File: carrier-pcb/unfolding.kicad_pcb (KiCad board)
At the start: 2 copper layers, 66 parts, among them J1 USB_C_Receptacle_USB2.0, J2 Conn_01x04_Female, J3 CONN_1-338068-8_TYC, U1 TCA9548APWR, U10 DRV2605LDGS, U11 DRV2605LDGS, U12 BMX160, U2 TCA9548APWR, U3 DRV2605LDGS, U4 DRV2605LDGS, U5 DRV2605LDGS, U6 DRV2605LDGS, U7 DRV2605LDGS, U8 DRV2605LDGS, U9 DRV2605LDGS

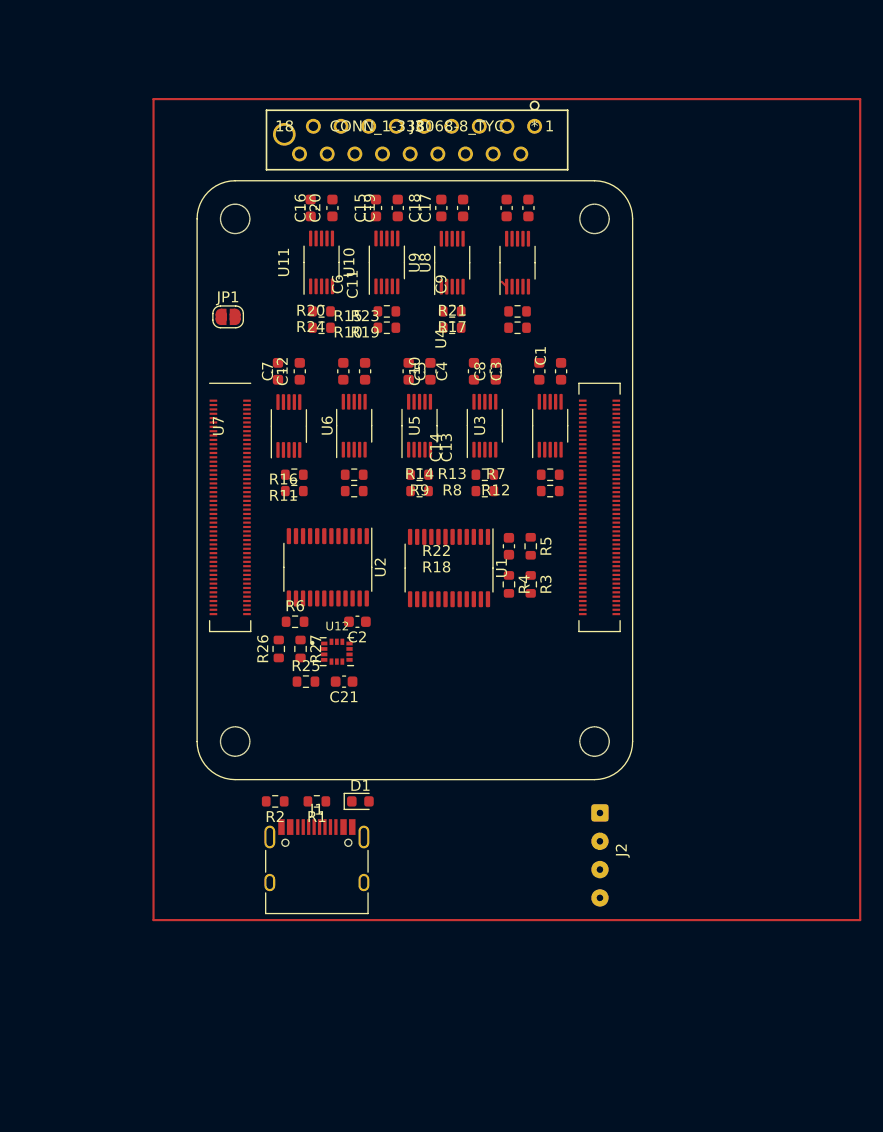
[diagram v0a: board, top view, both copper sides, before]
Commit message: removed more backups and renamed files. USE MORE BRANCHES, DONT RENAME
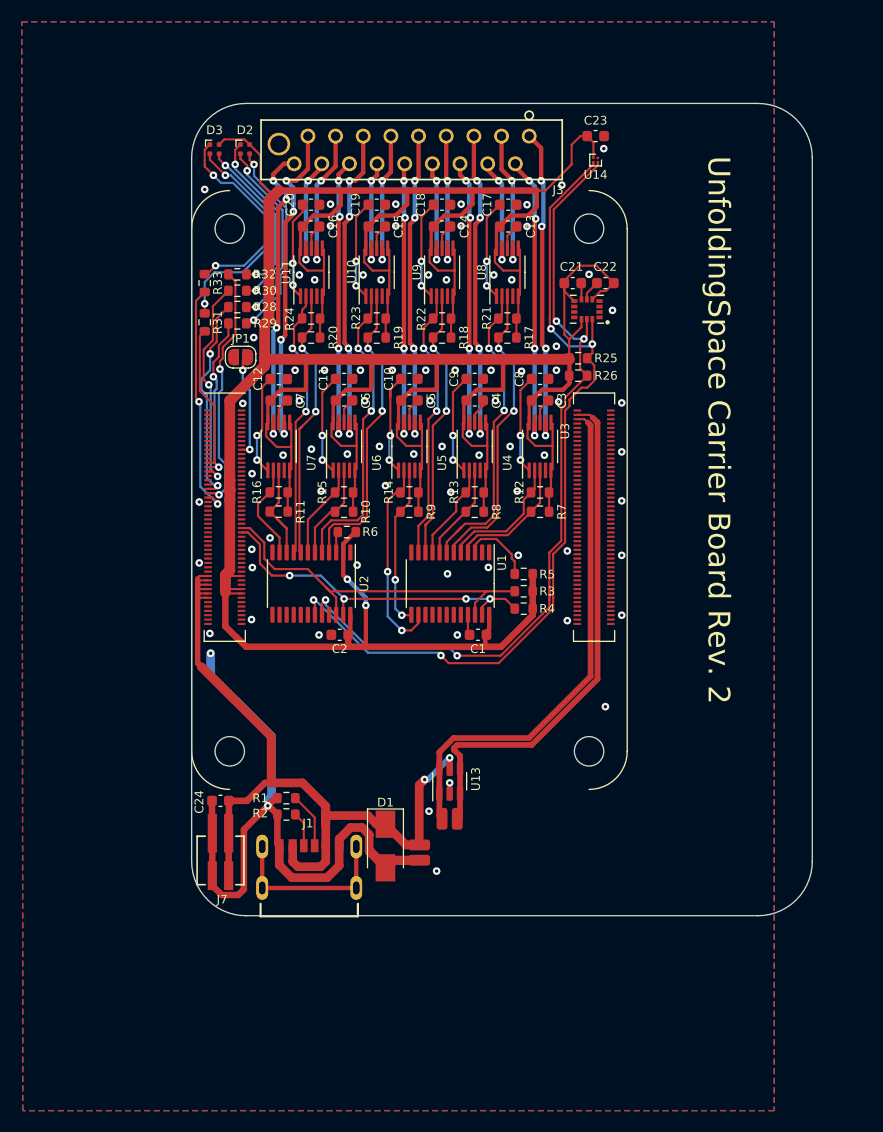
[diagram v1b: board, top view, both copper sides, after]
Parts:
- removed R27: 2K2, Resistor_SMD:R_0603_1608Metric
- added ?: , , F.Cu at (155.4, 37.8)
- added C22: 100n, Capacitor_SMD:C_0603_1608Metric, F.Cu at (153.0, 44.9)
- added C23: 2.2u, Capacitor_SMD:C_0603_1608Metric, F.Cu at (152.1, 31.4)
- added C24: 1u, Capacitor_SMD:C_0603_1608Metric, F.Cu at (117.7, 92.5)
- added D2: UHD1110-FKA, LED_SMD:LED_Lumex_SML-LX0404SIUPGUSB, F.Cu at (119.9, 32.6)
- added D3: UHD1110-FKA, LED_SMD:LED_Lumex_SML-LX0404SIUPGUSB, F.Cu at (117.1, 32.6)
- added J4: Conn_01x01_Female, Connector_Wire:SolderWirePad_1x01_SMD_1x2mm, F.Cu at (138.0, 94.1)
- added J5: Conn_01x01_Female, Connector_Wire:SolderWirePad_1x01_SMD_1x2mm, F.Cu at (139.4, 94.1)
- added J6: Conn_01x01_Female, Connector_Wire:SolderWirePad_1x01_SMD_1x2mm, F.Cu at (135.9, 97.9)
- added J7: Fan, Pico-Spox:PICOspox-2-v, F.Cu at (117.7, 97.2)
- added R28: 1K, Resistor_SMD:R_0603_1608Metric, F.Cu at (119.2, 47.1)
- added R29: 220, Resistor_SMD:R_0603_1608Metric, F.Cu at (119.2, 48.6)
- added R30: 150, Resistor_SMD:R_0603_1608Metric, F.Cu at (119.2, 45.6)
- added R31: 1K, Resistor_SMD:R_0603_1608Metric, F.Cu at (116.2, 48.5)
- added R32: 220, Resistor_SMD:R_0603_1608Metric, F.Cu at (119.2, 44.1)
- added R33: 150, Resistor_SMD:R_0603_1608Metric, F.Cu at (116.2, 44.9)
- added ToFCam-Stecker: ToFCam-Stecker, own:SteckerMicro-USB30-gewinkelt, F.Cu at (164.6, 95.9)
- added U13: WE 82400102, Package_TO_SOT_SMD:SOT-23-6, F.Cu at (138.7, 90.7)
- added U14: MMC5633NJL, Package_BGA:WLP-4_0.86x0.86mm_P0.4mm, F.Cu at (152.1, 33.6)
- D1: value RND SMBJ5A -> SMBJ5.0A; footprint Diode_SMD:D_0603_1608Metric -> Diode_SMD:D_SMA
- J1: value USB_C_Receptacle_USB2.0 -> USB4125-GF-A_REVA; footprint Connector_USB:USB_C_Receptacle_HRO_TYPE-C-31-M-12 -> USB4125-GF-A_REVA:GCT_USB4125-GF-A_REVA
- J2: value Conn_01x04_Female -> Conn_01x01_Female; footprint Connector_Wire:SolderWire-0.1sqmm_1x04_P3.6mm_D0.4mm_OD1mm -> Connector_Wire:SolderWirePad_1x01_SMD_1x2mm
- J3: value CONN_1-338068-8_TYC -> 1-338068-8
- U12: value BMX160 -> LSM6DSxx
- moved C21 42.2 mm to (150.0, 44.9), turned to 0 degrees
- moved U12 38.9 mm to (151.3, 47.3), turned to 180 degrees
- moved R25 38.8 mm to (150.5, 51.8)
- moved R26 37.2 mm to (150.5, 53.4), turned to 0 degrees
- moved J2 17.3 mm to (135.9, 96.5)
- moved R6 9.51 mm to (129.2, 67.8), turned to 180 degrees
- moved C1 8.61 mm to (141.3, 77.2), turned to 180 degrees
- moved D1 4.70 mm to (132.8, 96.6), turned to -90 degrees
- moved JP1 3.87 mm to (119.5, 51.7), turned to 180 degrees
- moved R7 3.52 mm to (147.0, 65.9)
- moved C7 3.30 mm to (123.0, 55.7), turned to 0 degrees
- moved C3 3.30 mm to (147.0, 55.7), turned to 0 degrees
- moved C4 3.30 mm to (141.0, 55.7), turned to 0 degrees
- moved C5 3.30 mm to (135.0, 55.7), turned to 0 degrees
- moved C6 3.30 mm to (129.0, 55.7), turned to 0 degrees
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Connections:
- net SCL_bmx160 renamed SCL_IMU
- net SDA_bmx160 renamed SDA_IMU
- D1 pad 1: GND -> +5V
- D1 pad 2: +5V -> GND
- J1 pad S1: unconnected-(J1-PadS1) -> Net-(J1-PadS1)
- J2 pad 1: GND -> +5V
- Module1 pad 25: unconnected-(Module1-Pad25) -> LED2R
- Module1 pad 27: unconnected-(Module1-Pad27) -> LED1G
- Module1 pad 29: unconnected-(Module1-Pad29) -> LED1B
- Module1 pad 37: unconnected-(Module1-Pad37) -> LED1R
- Module1 pad 39: unconnected-(Module1-Pad39) -> LED2G
- Module1 pad 41: unconnected-(Module1-Pad41) -> LED2B
- U12 pad 1: Net-(R27-Pad1) -> GND
- U5 pad 9: M5-. -> M5-
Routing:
- net +3V3: track 0.00 -> 379.1 mm, vias 0 -> 2
- net GND: track 0.00 -> 93.0 mm, vias 0 -> 78
- net +5V: track 0.00 -> 81.1 mm, vias 0 -> 2
- net SDA_IMU: track 0.00 -> 78.8 mm, vias 0 -> 4
- net SCL_IMU: track 0.00 -> 75.4 mm, vias 0 -> 4
- net USB_D-: track 0.00 -> 48.6 mm
- net USB_D+: track 0.00 -> 48.1 mm
- net SCL: track 0.00 -> 33.9 mm
- net SDA: track 0.00 -> 32.3 mm, vias 0 -> 4
- net M9+: track 0.00 -> 30.6 mm, vias 0 -> 4
- net M7+: track 0.00 -> 29.6 mm, vias 0 -> 4
- net M1+: track 0.00 -> 29.5 mm, vias 0 -> 4
- net M3+: track 0.00 -> 29.0 mm, vias 0 -> 4
- net M5+: track 0.00 -> 28.9 mm, vias 0 -> 4
- net SCL2: track 0.00 -> 28.6 mm, vias 0 -> 2
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- added copper zone on B.Cu, net GND
- added copper zone on F.Cu, net GND
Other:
- board outline added: 57 x 74.6 mm
- board text added: "UnfoldingSpace Carrier Board Rev. 2"

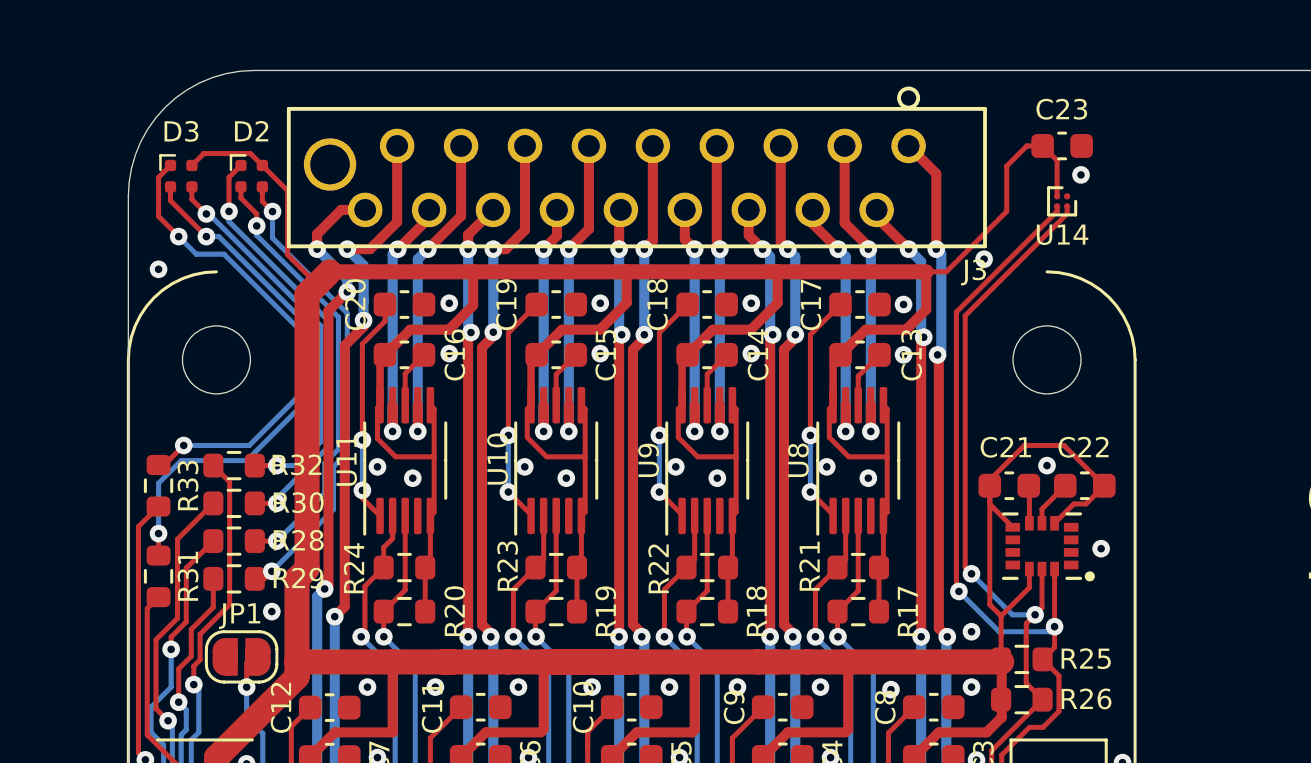
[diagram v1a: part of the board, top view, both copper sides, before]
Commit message: Changed RGB LED footprints
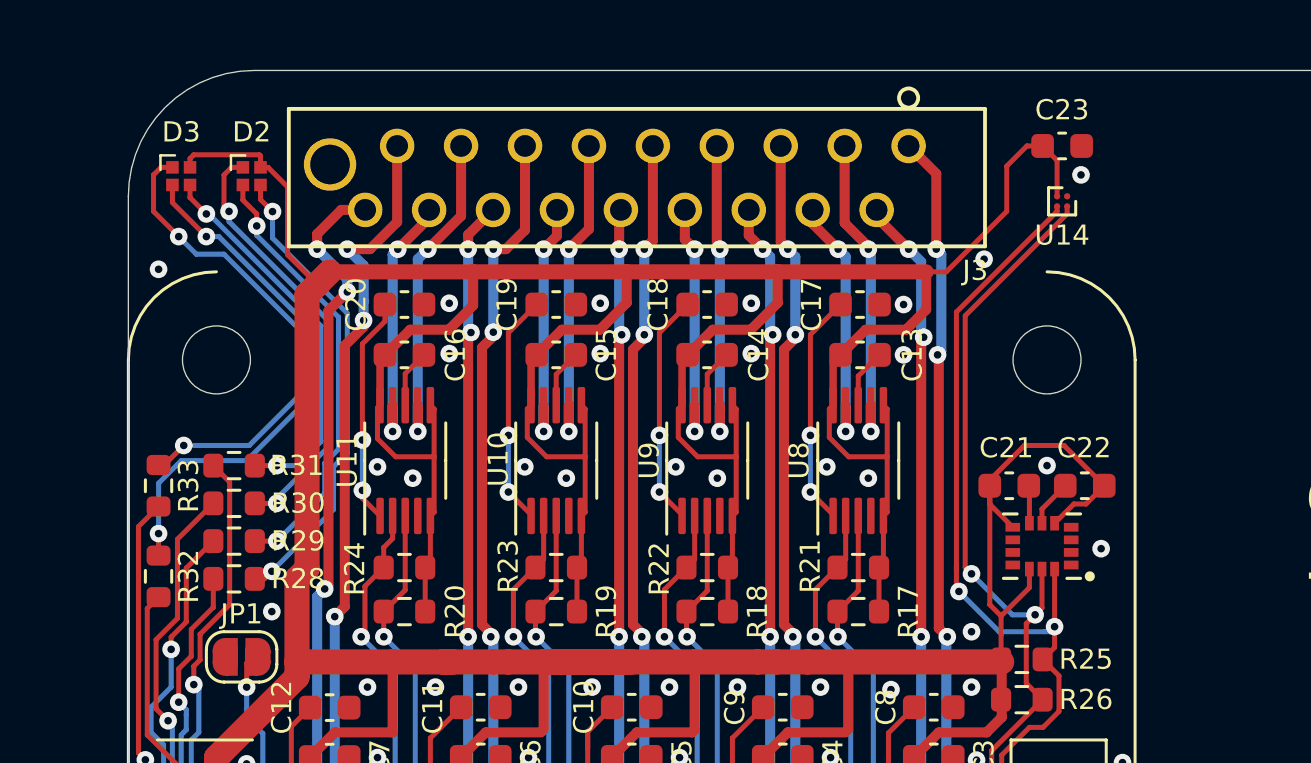
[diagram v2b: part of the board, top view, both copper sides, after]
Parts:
- removed ?: , 
- D2, D3: footprint LED_SMD:LED_Lumex_SML-LX0404SIUPGUSB -> RGBLED:UHD1110-FKA
- R28: renamed from R29; value 220 -> 1K
- R29: renamed from R28; value 1K -> 220
- R31: renamed from R32; value 220 -> 1K
- R32: renamed from R31; value 1K -> 220
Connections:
- D2 pad 2: +3V3 -> Net-(D2-Pad2)
- D2 pad 4: Net-(R28-Pad2) -> +3V3
- D3 pad 2: +3V3 -> Net-(D3-Pad2)
- D3 pad 4: Net-(R31-Pad2) -> +3V3
- Module1 pad 25: LED2R -> LED2G
- Module1 pad 27: LED1G -> LED1R
- Module1 pad 37: LED1R -> LED1G
- Module1 pad 39: LED2G -> LED2R
- R28 pad 1: LED1G -> LED1R
- R29 pad 1: LED1R -> LED1G
- R29 pad 2: Net-(R28-Pad2) -> Net-(D2-Pad2)
- R31 pad 1: LED2G -> LED2R
- R32 pad 1: LED2R -> LED2G
- R32 pad 2: Net-(R31-Pad2) -> Net-(D3-Pad2)
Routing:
- net Net-(D3-Pad2): track 0.00 -> 21.4 mm, vias 0 -> 2
- net Net-(R31-Pad2): track 21.3 -> 0.00 mm, vias 2 -> 0
- net Net-(D2-Pad2): track 0.00 -> 17.6 mm, vias 0 -> 2
- net Net-(R28-Pad2): track 17.6 -> 0.00 mm, vias 2 -> 0
- net LED2R: track 13.4 -> 22.9 mm, vias 0 -> 2
- net LED2G: track 22.9 -> 13.4 mm, vias 2 -> 0
- net LED1R: track 19.2 -> 15.1 mm
- net LED1G: track 15.1 -> 19.2 mm
- net +3V3: track 379.1 -> 379.7 mm

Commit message: Re-add non plated sot for rubber band for fixation of camera
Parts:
- added ?: , , F.Cu at (155.6, 38.0)
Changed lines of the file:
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@@
     )
+  )
+  (footprint "" (layer "F.Cu")
+    (at 155.6 38 90)
+    (fp_text reference "" (at 0 0 90) (layer "F.SilkS")
+      (effects (font (size 1.27 1.27) (thickness 0.15)))
+    )
+    (fp_text value "" (at 0 0 90) (layer "F.SilkS")
+      (effects (font (size 1.27 1.27) (thickness 0.15)))
+    )
+    (pad "" np_thru_hole oval locked (at 0 0 90) (size 3.4 1.2) (drill oval 3.4 1.2) (layers F&B.Cu *.Mask)
+      (solder_mask_margin 0.1) (clearance 0.1))
   )
   (footprint "Capacitor_SMD:C_0603_1608Metric" (layer "F.Cu")

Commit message: edit slot to min width of 1,6mm of aisler.net
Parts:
- moved ? 0.63 mm to (155.4, 37.4)
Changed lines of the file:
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@@
   )
   (footprint "" (layer "F.Cu")
-    (at 155.6 38 90)
+    (at 155.4 37.4 90)
     (fp_text reference "" (at 0 0 90) (layer "F.SilkS")
       (effects (font (size 1.27 1.27) (thickness 0.15)))
@@
       (effects (font (size 1.27 1.27) (thickness 0.15)))
     )
-    (pad "" np_thru_hole oval locked (at 0 0 90) (size 3.4 1.2) (drill oval 3.4 1.2) (layers F&B.Cu *.Mask)
+    (pad "" np_thru_hole oval locked (at 0 0 90) (size 3.4 1.6) (drill oval 3.4 1.6) (layers F&B.Cu *.Mask)
       (solder_mask_margin 0.1) (clearance 0.1))
   )
